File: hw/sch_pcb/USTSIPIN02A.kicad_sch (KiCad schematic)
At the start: 5 parts, among them M1 HOLE, M2 HOLE, M3 HOLE, M4 HOLE, M8 BMI-S-204-F

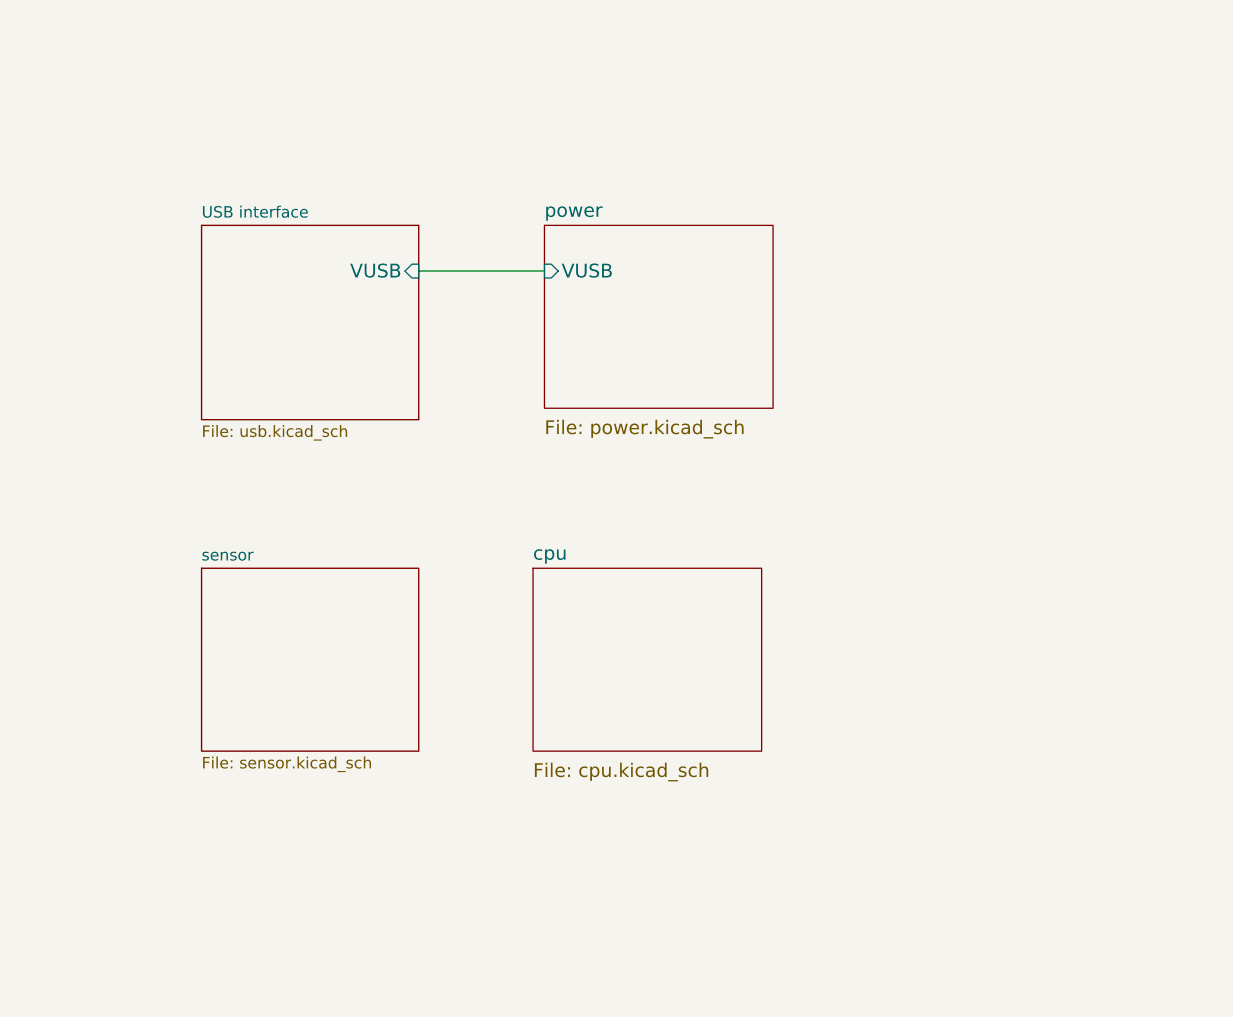
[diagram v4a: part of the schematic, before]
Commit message: Cleanup schematics Note polarity to ceramic capacitors.
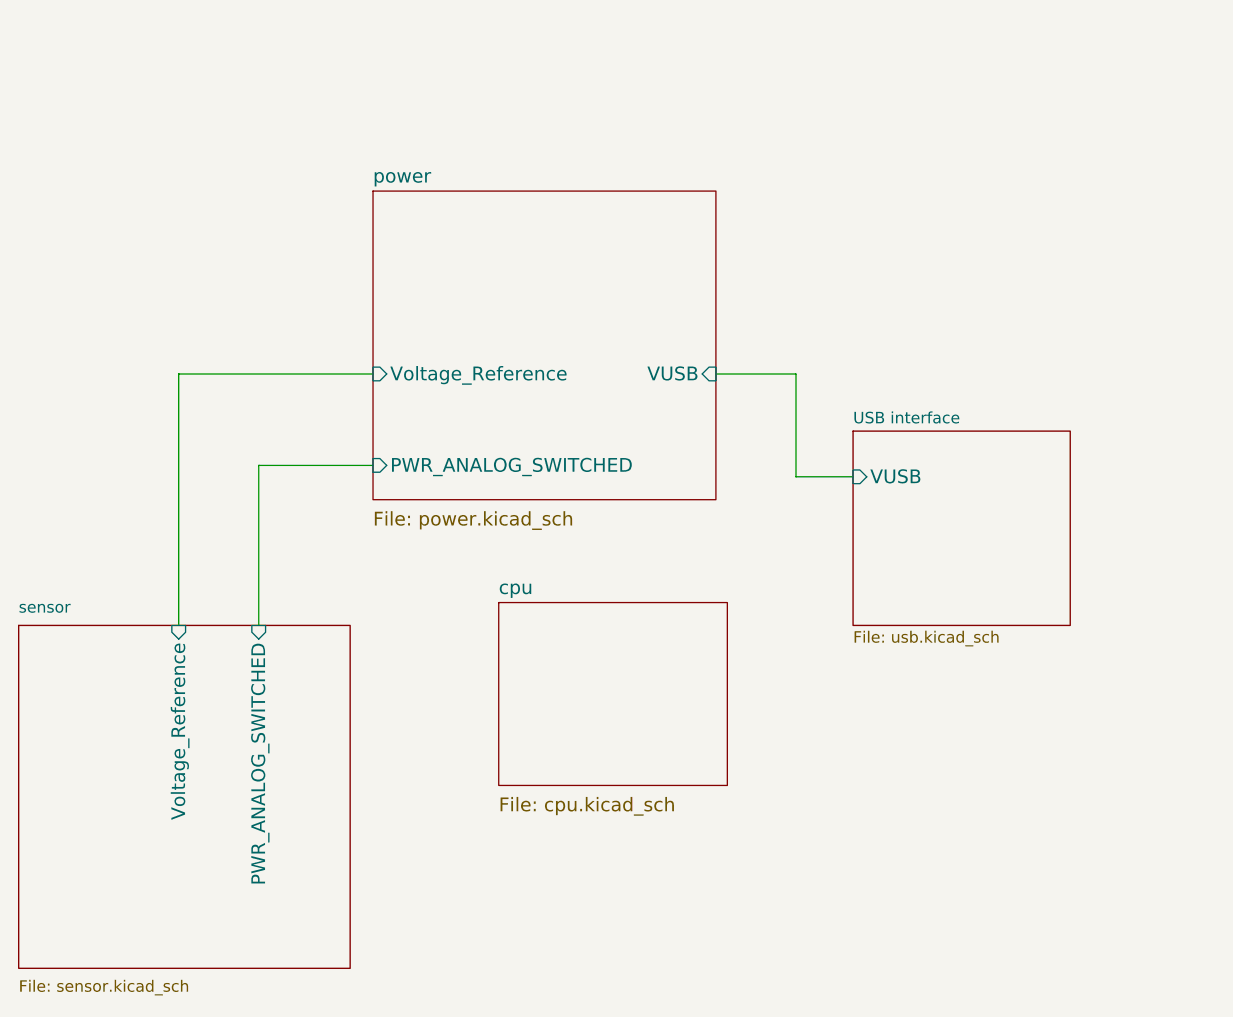
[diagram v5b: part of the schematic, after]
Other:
- sheet power ports: added PWR_ANALOG_SWITCHED, Voltage_Reference; removed none
- sheet sensor ports: added PWR_ANALOG_SWITCHED, Voltage_Reference; removed none

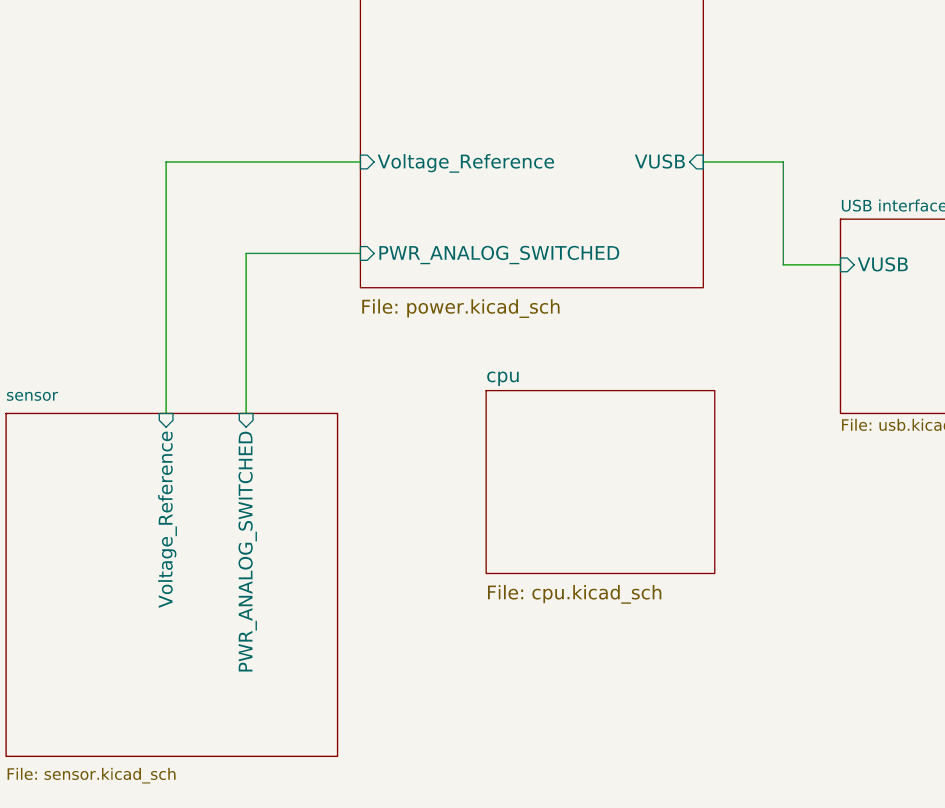
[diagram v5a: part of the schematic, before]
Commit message: Changed voltage reference to 0.9V.
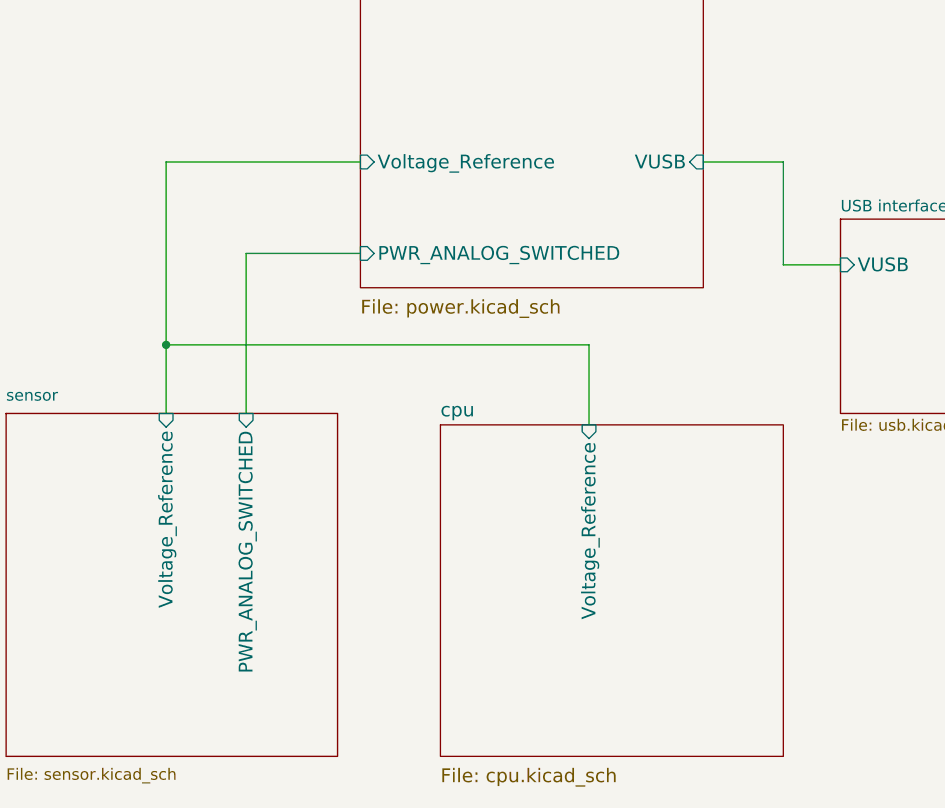
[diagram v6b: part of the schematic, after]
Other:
- sheet cpu ports: added Voltage_Reference; removed none
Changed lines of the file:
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@@
     (date "2022-05-22")
     (company "UST.cz")
-    (comment 2 "Silicon PIN diode based\\ndosimeter")
+    (comment 2 "Silicon PIN diode based\\ndosimeter and spectrometer")
     (comment 3 "info@ust.cz")
   )
+  (junction (at 63.5 82.55) (diameter 0) (color 0 0 0 0)
+  )
   (junction (at 257.81 16.51) (diameter 0) (color 0 0 0 0)
   )
@@
   (junction (at 267.97 16.51) (diameter 0) (color 0 0 0 0)
   )
-  (wire (pts (xy 63.5 90.17) (xy 63.5 62.23))
+  (wire (pts (xy 63.5 90.17) (xy 63.5 82.55))
+    (stroke (width 0) (type default) (color 0 0 0 0))
+  )
+  (wire (pts (xy 63.5 82.55) (xy 63.5 62.23))
     (stroke (width 0) (type default) (color 0 0 0 0))
   )
@@
     (stroke (width 0) (type default) (color 0 0 0 0))
   )
+  (wire (pts (xy 110.49 82.55) (xy 63.5 82.55))
+    (stroke (width 0) (type default) (color 0 0 0 0))
+  )
   (wire (pts (xy 252.73 17.78) (xy 252.73 16.51))
     (stroke (width 0) (type solid) (color 0 0 0 0))
@@
   (wire (pts (xy 262.89 16.51) (xy 267.97 16.51))
     (stroke (width 0) (type solid) (color 0 0 0 0))
+  )
+  (wire (pts (xy 110.49 91.44) (xy 110.49 82.55))
+    (stroke (width 0) (type default) (color 0 0 0 0))
   )
   (wire (pts (xy 257.81 16.51) (xy 257.81 17.78))
@@
     (pin "1")
   )
-  (sheet (at 99.06 87.63) (size 25.4 20.32)
+  (sheet (at 93.98 91.44) (size 38.1 36.83)
     (stroke (width 0) (type solid) (color 0 0 0 0))
     (fill (color 0 0 0 0.0000))
-    (property "Sheet name" "cpu" (id 0) (at 99.06 86.8675 0)
+    (property "Sheet name" "cpu" (id 0) (at 93.98 90.6775 0)
       (effects (font (size 1.524 1.524)) (justify left bottom))
     )
-    (property "Sheet file" "cpu.kicad_sch" (id 1) (at 99.06 109.22 0)
+    (property "Sheet file" "cpu.kicad_sch" (id 1) (at 93.98 129.54 0)
       (effects (font (size 1.524 1.524)) (justify left top))
+    )
+    (pin "Voltage_Reference" input (at 110.49 91.44 90)
+      (effects (font (size 1.524 1.524)) (justify right))
     )
   )
@@
     )
     (path "/00000000-0000-0000-0000-00005c69bcb4/49817ff0-d9f4-40df-983c-b127eda26390"
-      (reference "U3") (unit 1) (value "ISL21080DIH312Z-TK  1V25") (footprint "Package_TO_SOT_SMD:SOT-23")
+      (reference "U3") (unit 1) (value "ISL21080DIH309ZT") (footprint "Package_TO_SOT_SMD:SOT-23")
     )
     (path "/df946b97-ee48-4dc9-bb94-44edab77d662/0994f894-d9bb-4579-87be-ae742e824b9d"
